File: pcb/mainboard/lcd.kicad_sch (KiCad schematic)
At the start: 47 parts, among them J501 Conn_01x40_MountingPin, J502 Conn_01x06_MountingPin, J503 Conn_01x40_MountingPin, J504 Conn_01x28_MountingPin, U501 CAT4139, U502 SSD2828, U503 DS90C385A, U504 SM351LT, Y501 24MHz

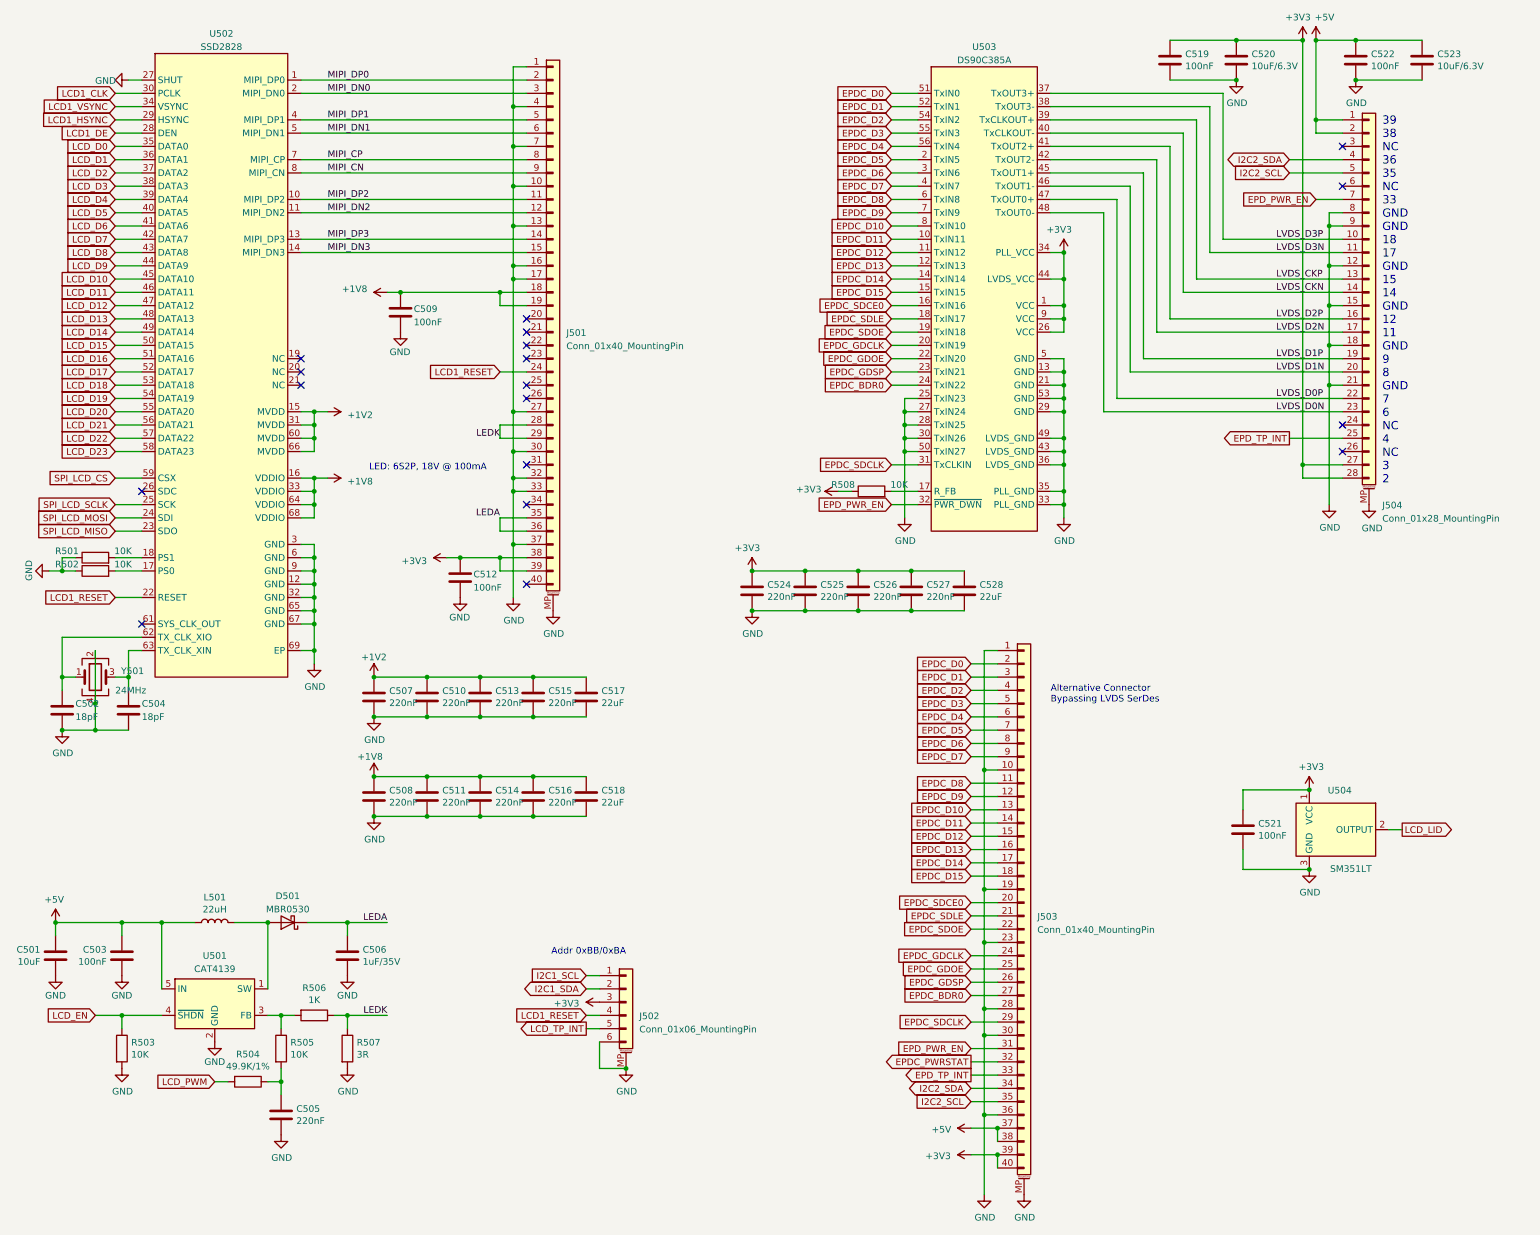
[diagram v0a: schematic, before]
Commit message: pcb: preliminary r0p1 schematics
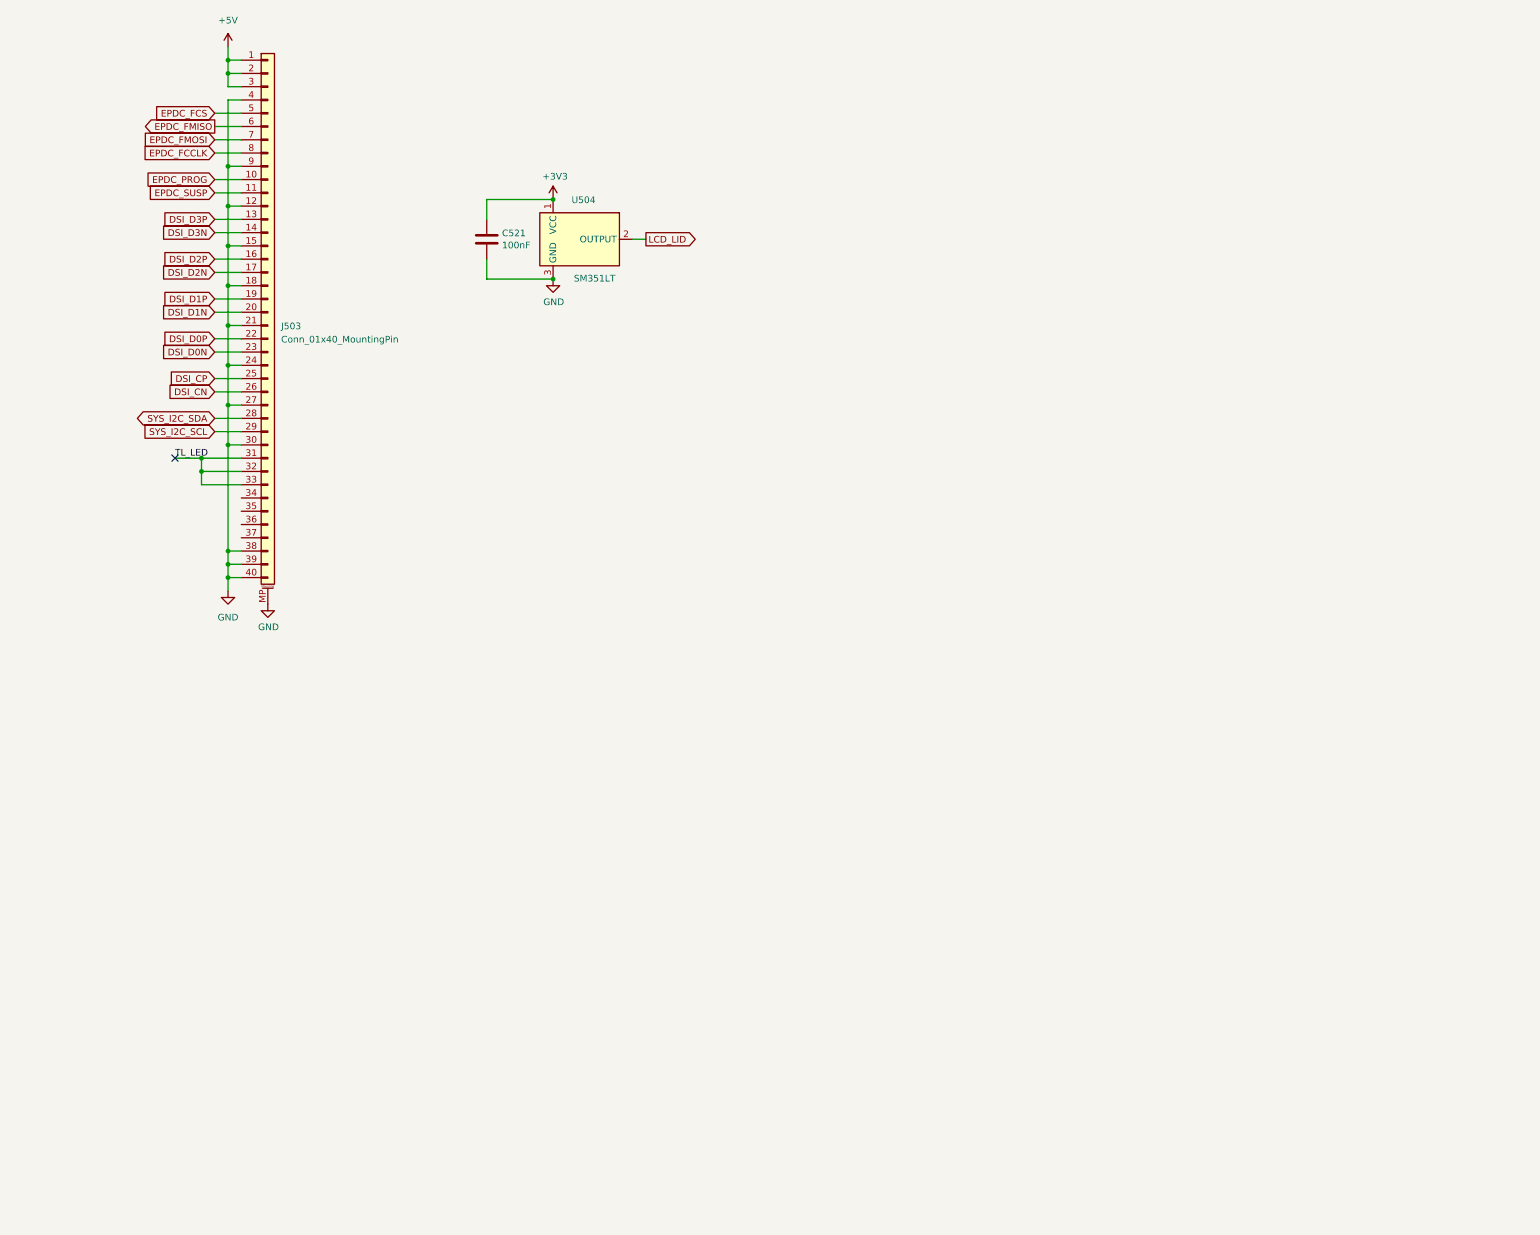
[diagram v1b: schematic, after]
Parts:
- removed C501: 10uF, Capacitor_SMD:C_0603_1608Metric, symbol Device:C
- removed C502, C504: 18pF, Capacitor_SMD:C_0402_1005Metric, symbol Device:C
- removed C503, C509, C512, C519, C522: 100nF, Capacitor_SMD:C_0402_1005Metric, symbol Device:C
- removed C505, C507, C508, C510, C511, C513, C514, C515, C516, C524, C525, C526, C527: 220nF, Capacitor_SMD:C_0402_1005Metric, symbol Device:C
- removed C506: 1uF/35V, Capacitor_SMD:C_0603_1608Metric, symbol Device:C
- removed C517, C518, C528: 22uF, Capacitor_SMD:C_0603_1608Metric, symbol Device:C
- removed C520, C523: 10uF/6.3V, Capacitor_SMD:C_0603_1608Metric, symbol Device:C
- removed D501: MBR0530, Diode_SMD:D_SOD-123, symbol Diode:MBR0530
- removed J501: Conn_01x40_MountingPin, Connector_FFC-FPC:Hirose_FH12-40S-0.5SH_1x40-1MP_P0.50mm_Horizontal, symbol Connector_Generic_MountingPin:Conn_01x40_MountingPin
- removed J502: Conn_01x06_MountingPin, Connector_FFC-FPC:Hirose_FH12-6S-0.5SH_1x06-1MP_P0.50mm_Horizontal, symbol Connector_Generic_MountingPin:Conn_01x06_MountingPin
- removed J504: Conn_01x28_MountingPin, Connector_FFC-FPC:Hirose_FH12-28S-0.5SH_1x28-1MP_P0.50mm_Horizontal, symbol Connector_Generic_MountingPin:Conn_01x28_MountingPin
- removed L501: 22uH, Inductor_SMD:L_Vishay_IHLP-1212, symbol Device:L
- removed R501, R502, R503, R505, R508: 10K, Resistor_SMD:R_0402_1005Metric, symbol Device:R
- removed R504: 49.9K/1%, Resistor_SMD:R_0402_1005Metric, symbol Device:R
- removed R506: 1K, Resistor_SMD:R_0402_1005Metric, symbol Device:R
- removed R507: 3R, Resistor_SMD:R_0402_1005Metric, symbol Device:R
- removed U501: CAT4139, Package_TO_SOT_SMD:SOT-23-5, symbol Regulator_Switching:AP3012
- removed U502: SSD2828, Package_DFN_QFN:QFN-68-1EP_8x8mm_P0.4mm_EP5.2x5.2mm_ThermalVias, symbol symbols:SSD2828
- removed U503: DS90C385A, Package_SO:TSSOP-56_6.1x14mm_P0.5mm, symbol symbols:DS90C385A
- removed Y501: 24MHz, Crystal:Crystal_SMD_3225-4Pin_3.2x2.5mm, symbol Device:Crystal_GND24
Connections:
- net EPDC_BDR0 is gone; now on net GND: J503.27 (Pin_27)
- net EPDC_D0 is gone; now on net +5V: J503.2 (Pin_2)
- net EPDC_D1 is gone; now on net +5V: J503.3 (Pin_3)
- net EPDC_D12 is gone; now on net GND: J503.15 (Pin_15)
- net EPDC_D15 is gone; now on net GND: J503.18 (Pin_18)
- net EPDC_D2 is gone; now on net GND: J503.4 (Pin_4)
- net EPDC_D7 is gone; now on net GND: J503.9 (Pin_9)
- net EPDC_D9 is gone; now on net GND: J503.12 (Pin_12)
- net EPDC_GDCLK is gone; now on net GND: J503.24 (Pin_24)
- net EPDC_SDLE is gone; now on net GND: J503.21 (Pin_21)
- net EPD_PWR_EN is gone; now on net TL_LED: J503.31 (Pin_31)
- net EPD_TP_INT is gone; now on net TL_LED: J503.33 (Pin_33)
- net +3V3: no longer J503.39 (Pin_39), J503.40 (Pin_40)
- net +5V: now also J503.1 (Pin_1); no longer J503.37 (Pin_37), J503.38 (Pin_38)
- net GND: now also J503.38 (Pin_38), J503.39 (Pin_39), J503.40 (Pin_40); no longer J503.1 (Pin_1), J503.10 (Pin_10), J503.19 (Pin_19), J503.23 (Pin_23), J503.28 (Pin_28), J503.36 (Pin_36)
- net EPDC_D10 renamed DSI_D3P
- net EPDC_D11 renamed DSI_D3N
- net EPDC_D13 renamed DSI_D2P
- net EPDC_D14 renamed DSI_D2N
- net EPDC_D3 renamed EPDC_FCS
- net EPDC_D4 renamed EPDC_FMISO
- net EPDC_D5 renamed EPDC_FMOSI
- net EPDC_D6 renamed EPDC_FCCLK
- net EPDC_D8 renamed EPDC_SUSP
- net EPDC_GDOE renamed DSI_CP
- net EPDC_GDSP renamed DSI_CN
- net EPDC_PWRSTAT renamed TL_LED
- net EPDC_SDCE0 renamed DSI_D1N
- net EPDC_SDCLK renamed SYS_I2C_SCL
- net EPDC_SDOE renamed DSI_D0P
- net I2C2_SCL: no longer names the net of J503.35 (Pin_35)
- net I2C2_SDA: no longer names the net of J503.34 (Pin_34)
- new net DSI_D0N: J503.23 (Pin_23)
- new net DSI_D1P: J503.19 (Pin_19)
- new net EPDC_PROG: J503.10 (Pin_10)
- new net SYS_I2C_SDA: J503.28 (Pin_28)
- no-connect marks 18 -> 1
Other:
- note removed: "39 38 NC 36 35 NC 33 GND GND 18 17 GND 15 14 GND 12 11 GND 9 8 GND 7 6 NC 4 NC 3 2"
- note removed: "Addr 0xBB/0xBA"
- note removed: "Alternative Connector Bypassing LVDS SerDes"
- note removed: "LED: 6S2P, 18V @ 100mA"
- company: Copyright EI-2030 2021. / Engineer: Wenting Zhang -> Copyright Modos 2021. / Engineer: Wenting Zhang
- moved on the sheet: C521, J503, U504

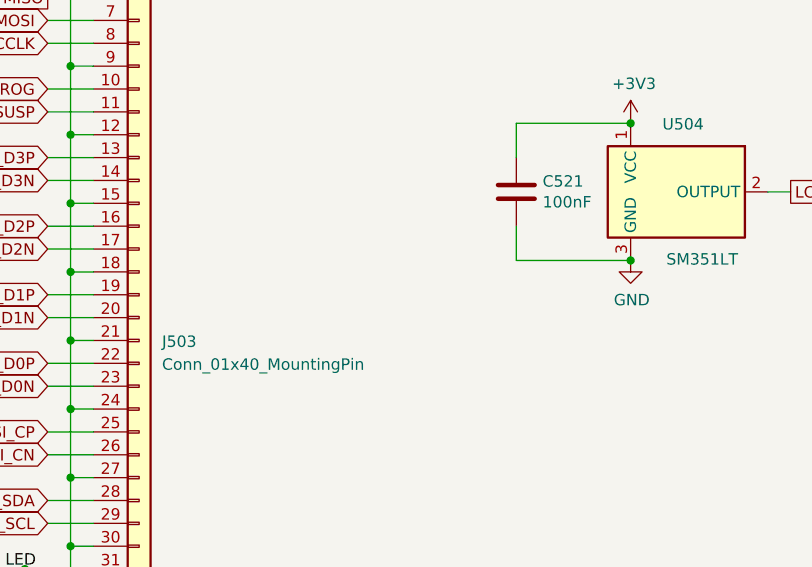
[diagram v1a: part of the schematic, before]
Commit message: pcb: initial placement for mb
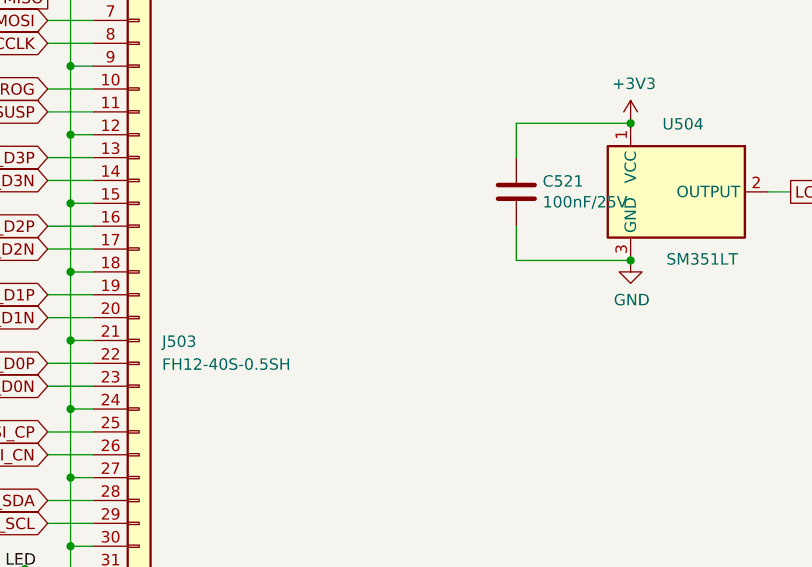
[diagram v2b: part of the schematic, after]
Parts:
- C521: value 100nF -> 100nF/25V; LCSC (none) -> C56392; Ref.Price (none) -> 0.0023
- J503: value Conn_01x40_MountingPin -> FH12-40S-0.5SH; LCSC (none) -> C376071; Ref.Price (none) -> 0.2405
- U504: LCSC (none) -> C80830; Ref.Price (none) -> 0.4112
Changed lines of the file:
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@@
   (symbol (lib_id "power:+5V") (at 121.92 46.99 0) (unit 1)
     (in_bom yes) (on_board yes) (fields_autoplaced)
-    (property "Reference" "#PWR?" (id 0) (at 121.92 50.8 0)
+    (property "Reference" "#PWR0108" (id 0) (at 121.92 50.8 0)
       (effects (font (size 1.27 1.27)) hide)
     )
@@
   (symbol (lib_id "power:GND") (at 121.92 151.13 0) (unit 1)
     (in_bom yes) (on_board yes) (fields_autoplaced)
-    (property "Reference" "#PWR?" (id 0) (at 121.92 157.48 0)
+    (property "Reference" "#PWR0109" (id 0) (at 121.92 157.48 0)
       (effects (font (size 1.27 1.27)) hide)
     )
@@
       (effects (font (size 1.27 1.27)) (justify left))
     )
-    (property "Value" "100nF" (id 1) (at 174.371 84.963 0)
+    (property "Value" "100nF/25V" (id 1) (at 174.371 84.963 0)
       (effects (font (size 1.27 1.27)) (justify left))
     )
@@
     )
     (property "Datasheet" "~" (id 3) (at 171.45 83.82 0)
+      (effects (font (size 1.27 1.27)) hide)
+    )
+    (property "LCSC" "C56392" (id 4) (at 171.45 83.82 0)
+      (effects (font (size 1.27 1.27)) hide)
+    )
+    (property "Ref.Price" "0.0023" (id 5) (at 171.45 83.82 0)
       (effects (font (size 1.27 1.27)) hide)
     )
@@
       (effects (font (size 1.27 1.27)) hide)
     )
+    (property "LCSC" "C80830" (id 4) (at 189.23 83.82 0)
+      (effects (font (size 1.27 1.27)) hide)
+    )
+    (property "Ref.Price" "0.4112" (id 5) (at 189.23 83.82 0)
+      (effects (font (size 1.27 1.27)) hide)
+    )
     (pin "1")
     (pin "2")
@@
       (effects (font (size 1.27 1.27)) (justify left))
     )
-    (property "Value" "Conn_01x40_MountingPin" (id 1) (at 132.08 102.9969 0)
+    (property "Value" "FH12-40S-0.5SH" (id 1) (at 132.08 102.9969 0)
       (effects (font (size 1.27 1.27)) (justify left))
     )
@@
       (effects (font (size 1.27 1.27)) hide)
     )
+    (property "LCSC" "C376071" (id 4) (at 129.54 97.79 0)
+      (effects (font (size 1.27 1.27)) hide)
+    )
+    (property "Ref.Price" "0.2405" (id 5) (at 129.54 97.79 0)
+      (effects (font (size 1.27 1.27)) hide)
+    )

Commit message: pcb: r0.1 mb routing done
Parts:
- added D501: RCLAMP3328P, Package_DFN_QFN:UDFN-9_1.0x3.8mm_P0.5mm, symbol Power_Protection:RCLAMP3328P
- added J501: HDMI_A, footprints:HDMI-D-Stripped, symbol Connector:HDMI_A
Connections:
- net +5V: now also J501.18 (+5V)
- net GND: now also D501.3 (A), J501.11 (CKS), J501.17 (GND), J501.2 (D2S), J501.5 (D1S), J501.8 (D0S), J501.SH
- net SYS_I2C_SCL renamed EPD_I2C_SCL
- net SYS_I2C_SDA renamed EPD_I2C_SDA
- removed net TL_LED: J503.31 (Pin_31), J503.32 (Pin_32), J503.33 (Pin_33)
- new net HDMI_HPD: J501.19 (HPD)
- new net HDMI_SCL: J501.15 (SCL)
- new net HDMI_SDA: J501.16 (SDA)
- new net HDMI_TX0N: D501.2 (K2), J501.9 (D0-)
- new net HDMI_TX0P: D501.8 (K7), J501.7 (D0+)
- new net HDMI_TX1N: D501.7 (K6), J501.6 (D1-)
- new net HDMI_TX1P: D501.4 (K3), J501.4 (D1+)
- new net HDMI_TX2N: D501.6 (K5), J501.3 (D2-)
- new net HDMI_TX2P: D501.5 (K4), J501.1 (D2+)
- new net HDMI_TXCN: D501.1 (K1), J501.12 (CK-)
- new net HDMI_TXCP: D501.9 (K8), J501.10 (CK+)
- no-connect marks 1 -> 3
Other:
- moved on the sheet: C521, U504
